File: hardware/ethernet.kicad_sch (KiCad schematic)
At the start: 98 parts, among them J5 USB_C_Receptacle, Q1 BSS138, Q2 BSS138, U11 TXS0202YZPR, U14 KSZ9031RNXCA, U4 CCGM1A1, X1 ECS-2520MV-250-xx

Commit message: Routing GPDI
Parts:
- C67, C68, C69, C70, C71, C72, C73, C74: now not fitted; now left out of the parts list
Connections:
- net +1V8: no longer C94.1, R125.1
- net +2V5: now also C94.1, R125.1
- net ID_SC: now also U4.J15 (IO_EA_B5)
- net ID_SD: now also U4.J16 (IO_EA_A5)
- net SCL0: now also U4.H15 (IO_EA_B6)
- net SDA0: now also U4.H16 (IO_EA_A6)
- net SD_DAT4: now also U4.G18 (IO_EA_A7)
- net SD_DAT5: now also U4.G17 (IO_EA_B7)
- net SD_DAT6: now also U4.G16 (IO_EA_A8)
- net SD_DAT7: now also U4.G15 (IO_EA_B8)
- no-connect marks 8 -> 3
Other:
- moved on the sheet: BTN1, BTN2, BTN3, C118, D3, D4, D5, D6, D7, D8, J5, Q1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

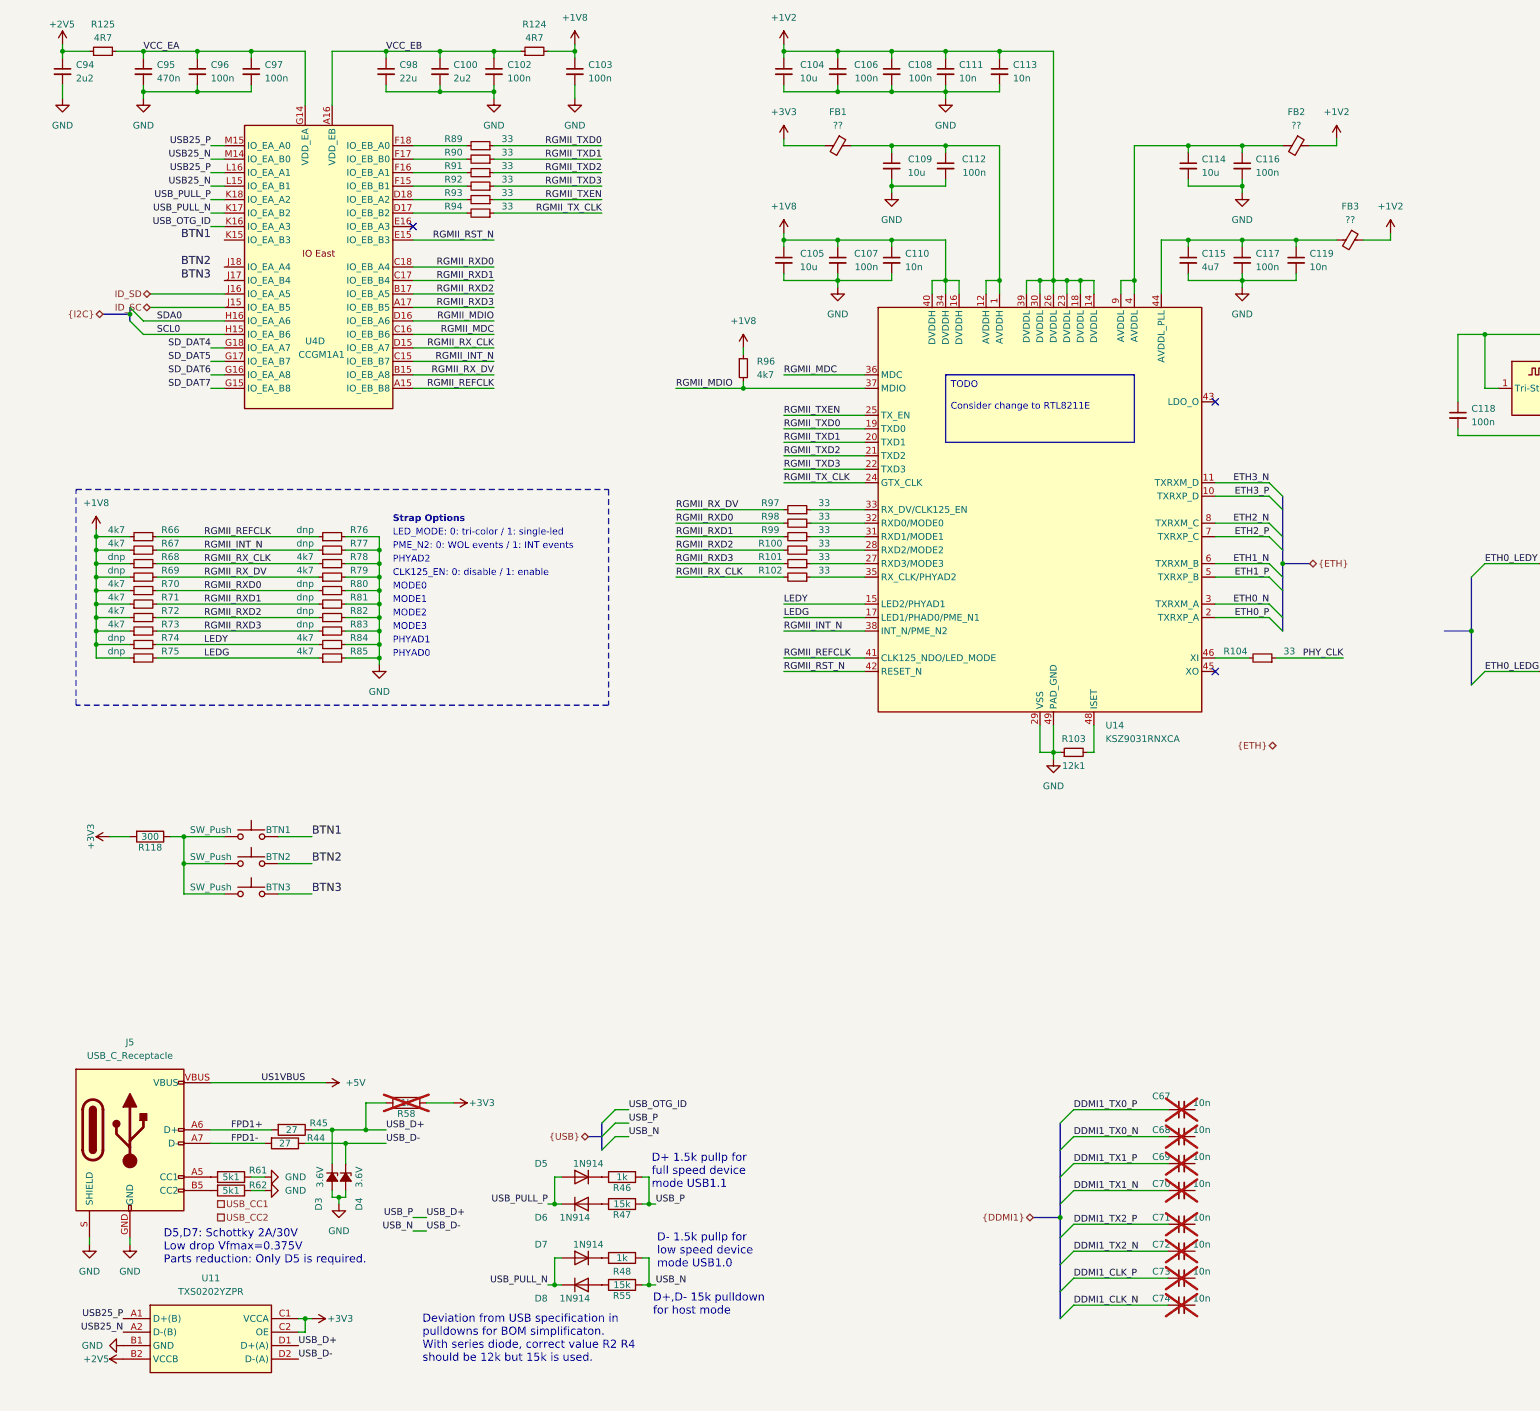
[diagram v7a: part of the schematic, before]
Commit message: Clearing ERC errors/warnings
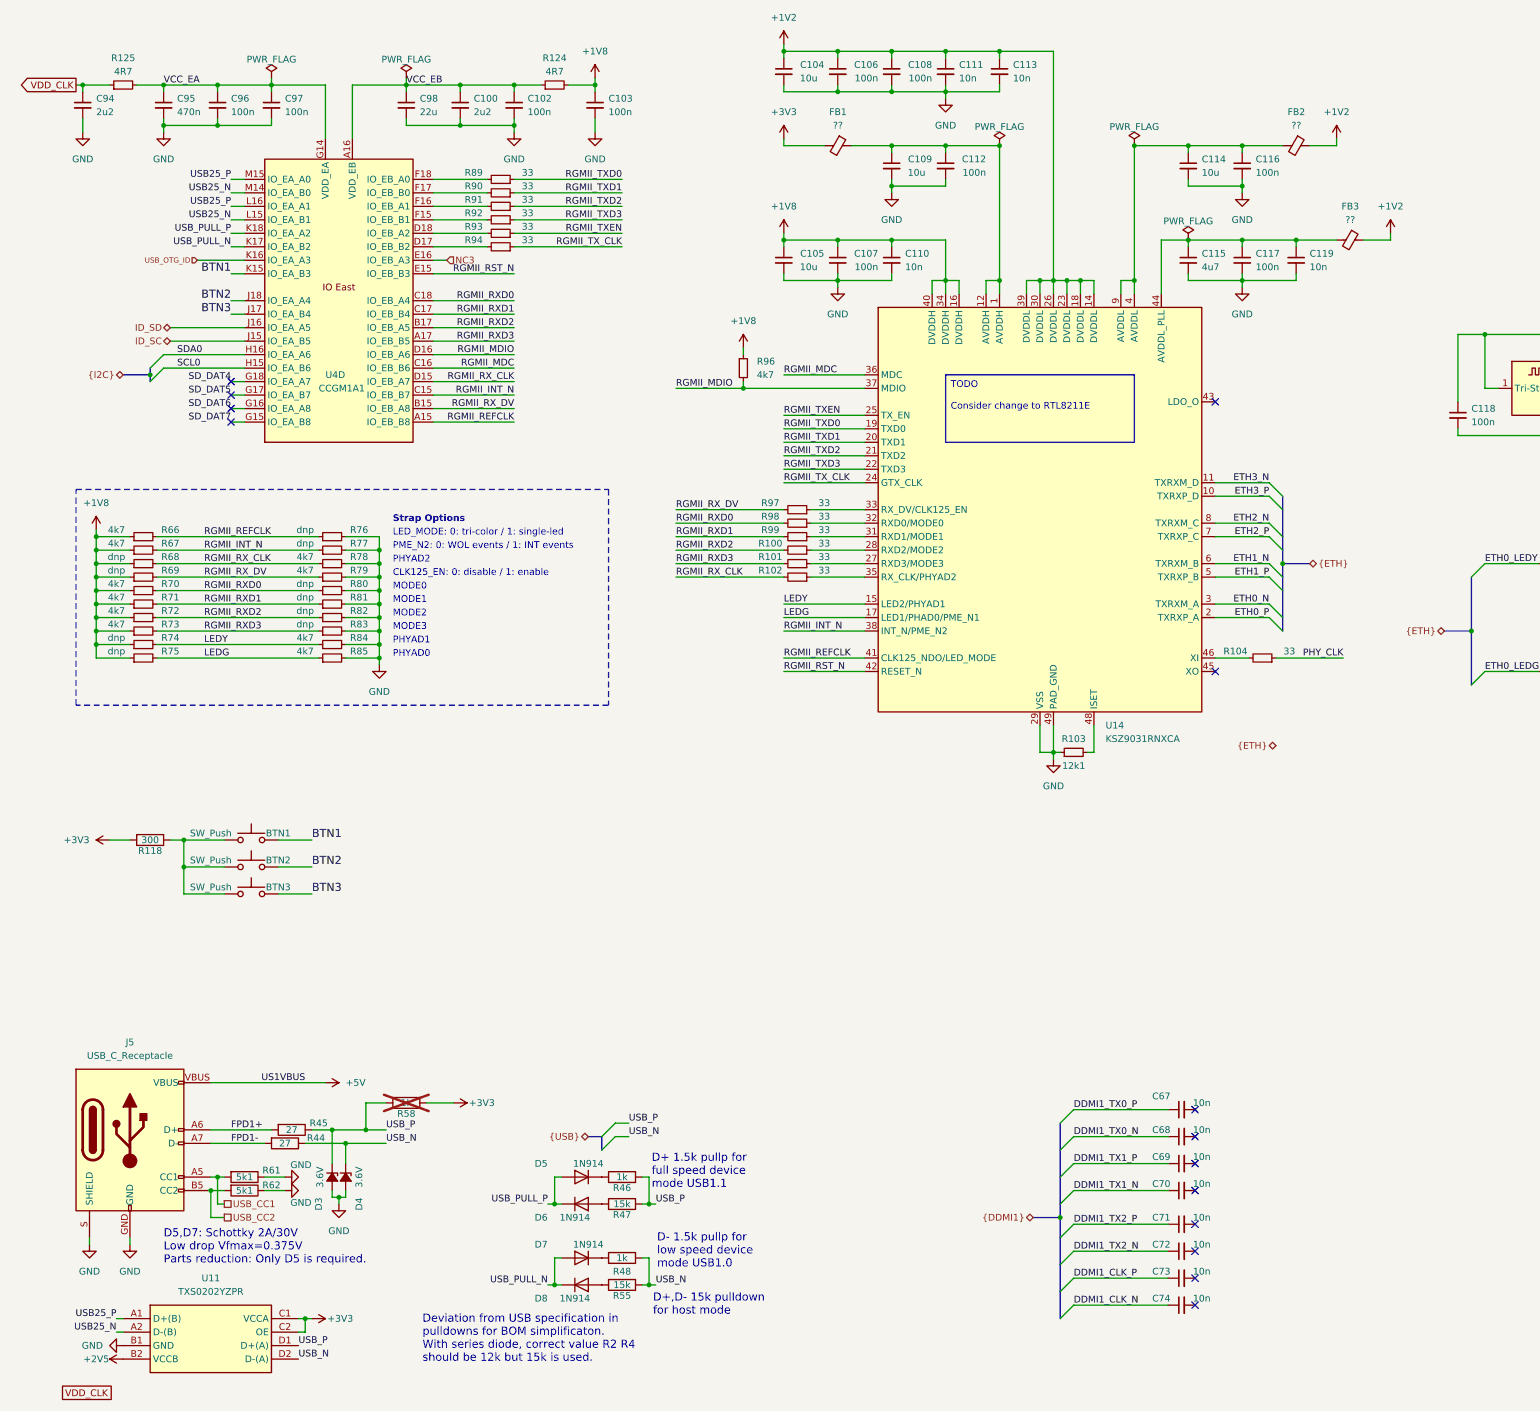
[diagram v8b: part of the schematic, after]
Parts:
- C67, C68, C69, C70, C71, C72, C73, C74: now fitted; now in the parts list
- D3, D4: symbol USB-rescue:D_Zener_Small_ALT-Device -> Device:D_Zener_Small_Filled
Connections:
- net +2V5: no longer C94.1, R125.1
- net BTN1: now also U4.K15 (IO_EA_B3)
- net BTN2: now also U4.J18 (IO_EA_A4)
- net BTN3: now also U4.J17 (IO_EA_B4)
- net USB_CC1: now also J5.A5 (CC1), R61.2
- net USB_CC2: now also J5.B5 (CC2), R62.2
- net NC3: now reaches U4.E16 (IO_EB_A3)
- net USB_D+ renamed USB_P
- net USB_D- renamed USB_N
- new net VDD_CLK: C94.1, R125.1
- no-connect marks 3 -> 14
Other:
- moved on the sheet: BTN1, BTN2, C100, C102, C103, C94, C95, C96, C97, C98, R118, R124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
